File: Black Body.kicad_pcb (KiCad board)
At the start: 2 copper layers, 52 x 53.5 mm, 39 parts, among them IC2 MCP96L00T-E_MX, J1 53307-2471, J2 Conn_01x02, J3 Conn_01x04, J4 Conn_02x08_Top_Bottom, J5 Conn_01x06

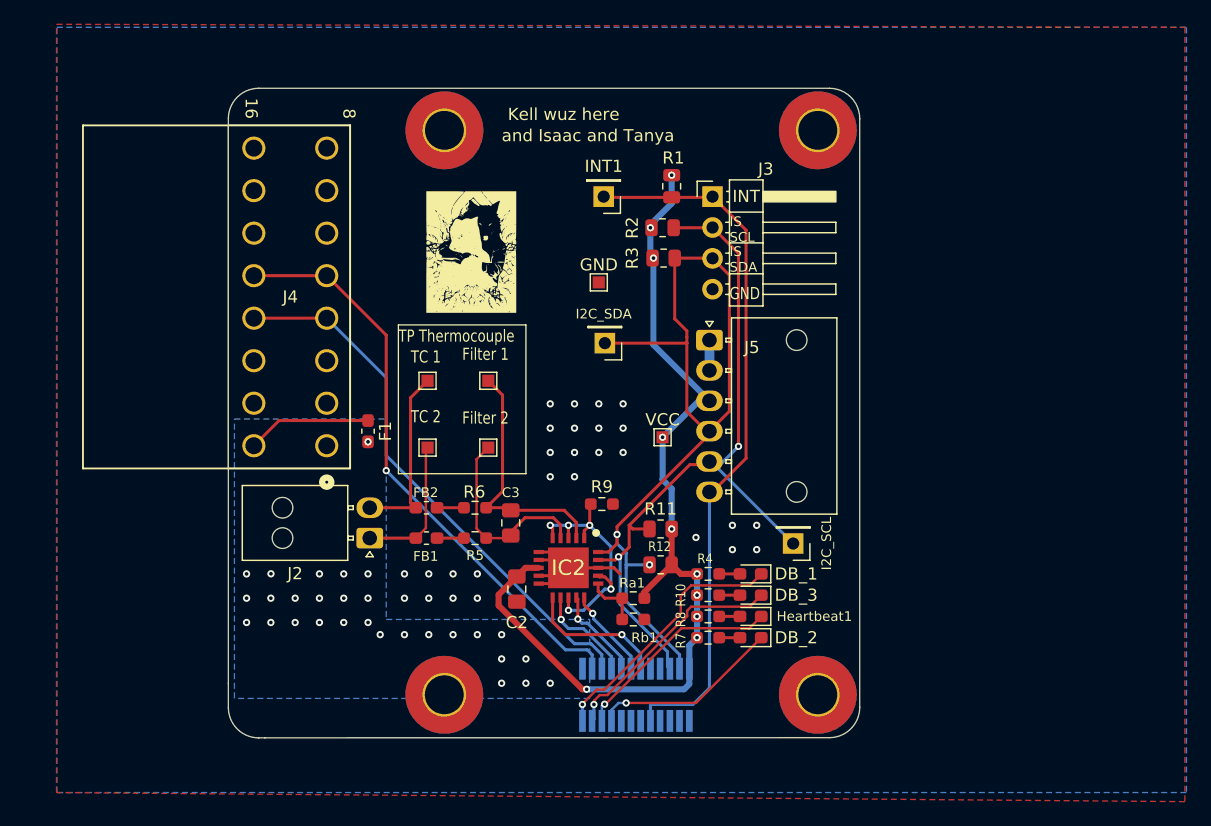
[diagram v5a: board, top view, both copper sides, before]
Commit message: updated layout
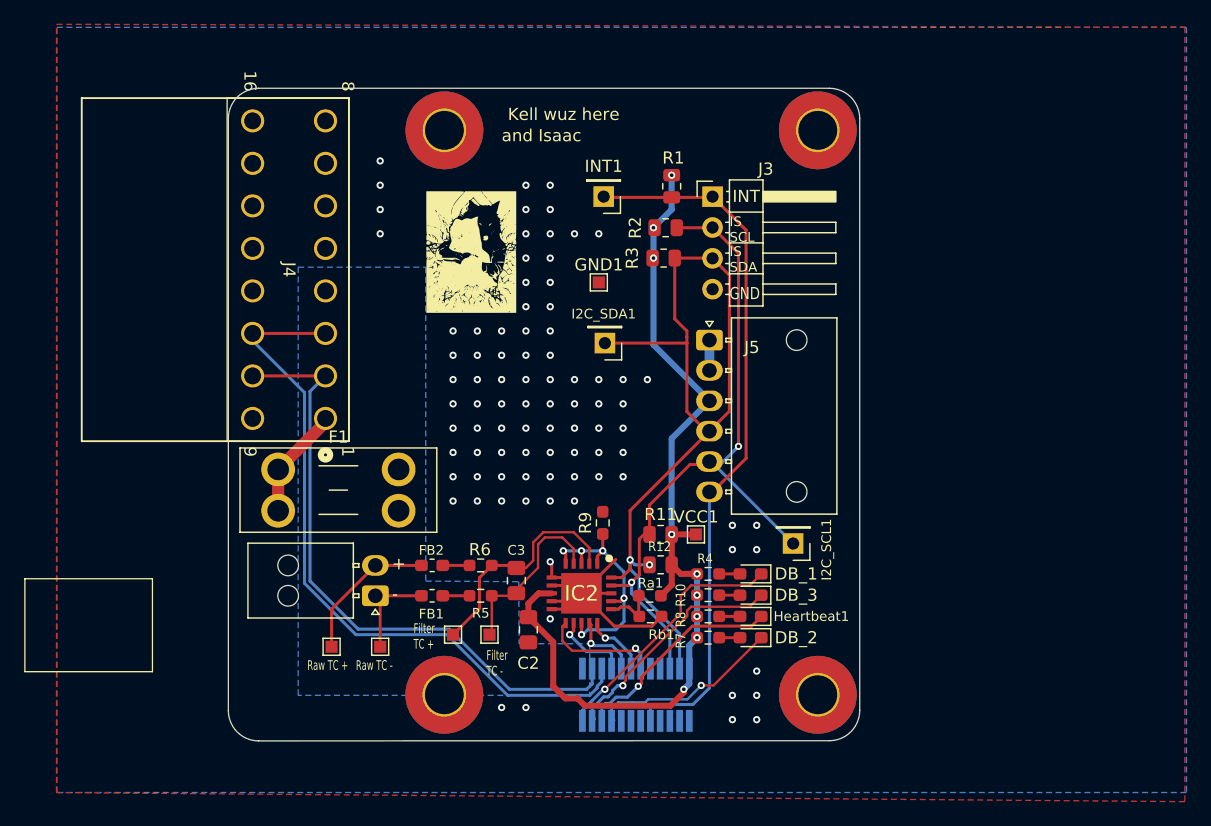
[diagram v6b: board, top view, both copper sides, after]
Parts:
- F1: footprint Fuse:Fuse_0603_1608Metric_Pad1.05x0.95mm_HandSolder -> Fuse:Fuseholder_Blade_Mini_Keystone_3568
- J1: footprint UTSVT_Connectors:PeripheralSOM -> UTSVT-Conn:PeripheralSOM
- J4: value Conn_02x08_Top_Bottom -> MX150_02x08_RightAngle; footprint UTSVT_Connectors:CONN_SD-75900-001_2X08_MOL -> UTSVT-Conn:CONN_SD-75900-001_2X08_MOL
- moved TP_TC_2 23.3 mm to (86.0, 113.0)
- moved TP_TC_F_2 21.1 mm to (96.0, 112.0)
- moved TP_TC_1 16.9 mm to (90.0, 113.0)
- moved TP_TC_F_1 15.4 mm to (99.0, 112.0)
- moved VCC1 8.46 mm to (116.0, 103.8)
- moved F1 8.04 mm to (81.6, 98.4), turned to 0 degrees
- moved C3 4.77 mm to (101.2, 107.5)
- moved FB1 4.77 mm to (94.3, 108.8)
- moved FB2 4.77 mm to (94.3, 106.3)
- moved J2 4.77 mm to (89.6, 108.8)
- moved R5 4.77 mm to (98.3, 108.8)
- moved R6 4.77 mm to (98.3, 106.3)
- moved C2 3.48 mm to (102.2, 111.6)
- moved IC2 2.36 mm to (106.6, 108.6)
- moved J4 2.25 mm to (82.5, 82.0)
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- renumbered GND to GND1, I2C_SCL to I2C_SCL1, I2C_SDA to I2C_SDA1, VCC to VCC1
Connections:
- F1 pad 1: Net-(J4-Pin_9) -> Net-(J4-+24V)
- J4 pad 1: +24V -> Net-(J4-+24V)
- J4 pad 10: unconnected-(J4-Pin_10-Pad10) -> /CAN_H
- J4 pad 11: unconnected-(J4-Pin_11-Pad11) -> /CAN_L
- J4 pad 12: /CAN_L -> GND
- J4 pad 13: /CAN_H -> unconnected-(J4-Pad13)
- J4 pad 16: GND -> unconnected-(J4-Pad16)
- J4 pad 2: unconnected-(J4-Pin_2-Pad2) -> /CAN_H
- J4 pad 3: unconnected-(J4-Pin_3-Pad3) -> /CAN_L
- J4 pad 4: /CAN_L -> +24V
- J4 pad 5: /CAN_H -> unconnected-(J4-Pad5)
- J4 pad 8: GND -> unconnected-(J4-Pad8)
- J4 pad 9: Net-(J4-Pin_9) -> GND
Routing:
- net /CAN_L: track 45.0 -> 58.3 mm
- net Net-(J4-Pin_9): track 10.3 -> 0.00 mm
- net Net-(J4-+24V): track 0.00 -> 9.22 mm
- net /CAN_H: track 48.5 -> 52.3 mm, vias 1 -> 0
- net Net-(J2-Pin_1): track 11.5 -> 7.97 mm
- net Net-(J2-Pin_2): track 14.7 -> 11.7 mm
- net /I2C1_SCL: track 62.0 -> 59.5 mm
- net GND: track 21.1 -> 23.4 mm, vias 27 -> 88
- net /Alert_2: track 8.39 -> 6.48 mm
- net /Alert_4: track 7.44 -> 5.54 mm
- net /Alert_3: track 7.65 -> 5.76 mm
- net /Alert_1: track 11.6 -> 9.95 mm
- net Net-(IC2-VIN+): track 20.7 -> 19.4 mm
- net Net-(IC2-VIN-): track 16.9 -> 15.6 mm
- net +3V3: track 76.5 -> 75.7 mm, vias 10 -> 9
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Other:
- board size 52 x 53.5 mm -> 52 x 53.7 mm
- board text added: "+"
- board text added: "-"
- board text added: "Filter TC +"
- board text added: "Filter TC -"
- board text added: "Raw TC +"
- board text added: "Raw TC -"
- board text added: "and Isaac"
- board text removed: "Filter 1"
- board text removed: "Filter 2"
- board text removed: "TC 1"
- board text removed: "TC 2"
- board text removed: "TP Thermocouple"
- board text removed: "and Isaac and Tanya"
